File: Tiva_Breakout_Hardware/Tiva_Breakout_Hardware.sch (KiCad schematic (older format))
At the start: 8 parts, among them U1 TM4C129E_Launchpad

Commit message: Finished 30V LEDs and connectors
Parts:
- added D10, D11, D2, D3, D4, D5, D6, D7, D8, D9: 3V3_LED, LED_SMD:LED_0603_1608Metric_Pad1.05x0.95mm_HandSolder, symbol Device:LED_Small
- added R10, R11, R2, R3, R4, R5, R6, R7, R8, R9: 330, Resistor_SMD:R_0603_1608Metric_Pad1.05x0.95mm_HandSolder, symbol Device:R
- 12V_A1: renamed from 12V_B2; value Molex_SL_04 -> PH_2x5; footprint MRDT_Connectors:MOLEX_SL_04_Horizontal -> Connector_PinHeader_1.27mm:PinHeader_2x05_P1.27mm_Vertical; symbol Tiva_Breakout_Hardware-rescue:Molex_SL_04-MRDT_Connectors -> Connector_Generic:Conn_02x05_Odd_Even
- Conn30V_L1: value Molex_SL_07 -> PH_2x5; footprint MRDT_Connectors:MOLEX_SL_07_Horizontal -> Connector_PinHeader_1.27mm:PinHeader_2x05_P1.27mm_Vertical; symbol MRDT_Connectors:Molex_SL_07 -> Connector_Generic:Conn_02x05_Odd_Even
- Conn30V_R1: value Molex_SL_08 -> PH_2x5; footprint MRDT_Connectors:MOLEX_SL_08_Horizontal -> Connector_PinHeader_1.27mm:PinHeader_2x05_P1.27mm_Vertical; symbol MRDT_Connectors:Molex_SL_08 -> Connector_Generic:Conn_02x05_Odd_Even
- ConnPCH_C2: value Molex_SL_10 -> PH_2x5; footprint MRDT_Connectors:MOLEX_SL_10_Horizontal -> Connector_PinHeader_1.27mm:PinHeader_2x05_P1.27mm_Vertical; symbol Tiva_Breakout_Hardware-rescue:Molex_SL_10-MRDT_Connectors -> Connector_Generic:Conn_02x05_Odd_Even
- R1: symbol Device:R_Small -> Device:R
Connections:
- net GND: now also D10.1 (K), D11.1 (K), D2.1 (K), D3.1 (K), D4.1 (K), D5.1 (K), D6.1 (K), D7.1 (K), D8.1 (K), D9.1 (K)
- net AUX_EN: now reaches U1.PC4 (A1_3)
- net AUX_EN: now also Conn30V_R1.6 (Pin_6), R8.2
- net at U1.PC5 (A1_4): no longer 12V_A1.1
- net at U1.PC6 (A1_5): no longer 12V_A1.2
- net at U1.PD3 (A1_7): no longer 12V_A1.4
- net RKT_ISENSE: now reaches U1.PE4 (A1_2)
- net RKT_ISENSE: now also Conn30V_R1.4 (Pin_4)
- net at U1.PE5 (A1_6): no longer 12V_A1.3
- net at U1.PF1 (C1_1): no longer ConnPCH_C2.1
- net at U1.PF2 (C1_2): no longer ConnPCH_C2.2
- net at U1.PF3 (C1_3): no longer ConnPCH_C2.3
- net at U1.PG0 (C1_4): no longer ConnPCH_C2.4
- net at U1.PL0 (C1_7): no longer ConnPCH_C2.7
- net at U1.PL1 (C1_8): no longer ConnPCH_C2.8
- net at U1.PL2 (C1_9): no longer ConnPCH_C2.9
- net at U1.PL3 (C1_10): no longer ConnPCH_C2.10
- net at U1.PL4 (C1_5): no longer ConnPCH_C2.5
- net at U1.PL5 (C1_6): no longer ConnPCH_C2.6
- net M5_EN: now reaches U1.PD5 (A2_6)
- net M5_EN: now also Conn30V_L1.9 (Pin_9), R6.2
- net M1_EN: now reaches U1.PN4 (A2_10)
- net M1_EN: now also Conn30V_L1.8 (Pin_8), R2.2
- net M2_EN: now reaches U1.PN5 (A2_9)
- net M2_EN: now also Conn30V_L1.4 (Pin_4), R3.2
- net M3_EN: now reaches U1.PP4 (A2_8)
- net M3_EN: now also Conn30V_L1.1 (Pin_1), R4.2
- net M4_EN: now reaches U1.PQ0 (A2_7)
- net M4_EN: now also Conn30V_L1.5 (Pin_5), R5.2
- net M3_ISENSE: now reaches Conn30V_L1.2 (Pin_2), U1.PB4 (B2_3)
- net M2_ISENSE: now reaches U1.PB5 (B2_4)
- net M2_ISENSE: now also Conn30V_L1.6 (Pin_6); no longer Conn30V_L1.3
- net M1_ISENSE: now reaches U1.PK0 (B2_5)
- net M1_ISENSE: now also Conn30V_L1.10 (Pin_10); no longer Conn30V_L1.4
- net M5_ISENSE: now reaches U1.PK1 (B2_6)
- net M5_ISENSE: now also Conn30V_L1.7 (Pin_7); no longer Conn30V_L1.5
- net M4_ISENSE: now reaches U1.PK2 (B2_7)
- net M4_ISENSE: now also Conn30V_L1.3 (Pin_3); no longer Conn30V_L1.6
- net at U1.PK3 (B2_8): no longer Conn30V_L1.7
- net 12V_CURR renamed 12V_EN
- net 12V_EN: now also Conn30V_R1.10 (Pin_10), R9.2; no longer Conn30V_R1.4
- net 12V_ON renamed M6_EN
- net M6_EN: now also R11.2
- net AUX_CURR renamed 12V_ISENSE
- net 12V_ISENSE: now also Conn30V_R1.9 (Pin_9); no longer Conn30V_R1.6
- net AUX_ON renamed SP_EN
- net SP_EN: now also Conn30V_R1.7 (Pin_7), R10.2; no longer Conn30V_R1.5
- net EX_CURR renamed AUX_ISENSE
- net AUX_ISENSE: now also Conn30V_R1.8 (Pin_8); no longer Conn30V_R1.2
- net EX_ON renamed M6_ISENSE
- net M6_ISENSE: now also U1.PD7 (B1_7); no longer U1.PM5 (B1_10)
- net RKT_CURR renamed SP_ISENSE
- net SP_ISENSE: now also Conn30V_R1.5 (Pin_5); no longer Conn30V_R1.8
- removed net RKT_ON: Conn30V_R1.7, U1.PD7 (B1_7)
- new net: D2.2 (A), R2.1
- new net: D3.2 (A), R3.1
- new net: D4.2 (A), R4.1
- new net: D5.2 (A), R5.1
- new net: D6.2 (A), R6.1
- new net: D7.2 (A), R7.1
- new net: D8.2 (A), R8.1
- new net: D9.2 (A), R9.1
- new net: D10.2 (A), R10.1
- new net: D11.2 (A), R11.1
- new net RKT_EN: Conn30V_R1.2 (Pin_2), R7.2, U1.PM5 (B1_10)
- no-connect marks 47 -> 39
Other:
- note added: "30V_L"
- note removed: "ACT_CRRT"
- note removed: "ACT_CTRL"
- note removed: "LOG_CRRT"
- note removed: "LOG_CTRL"
- moved on the sheet: U1E, U1F

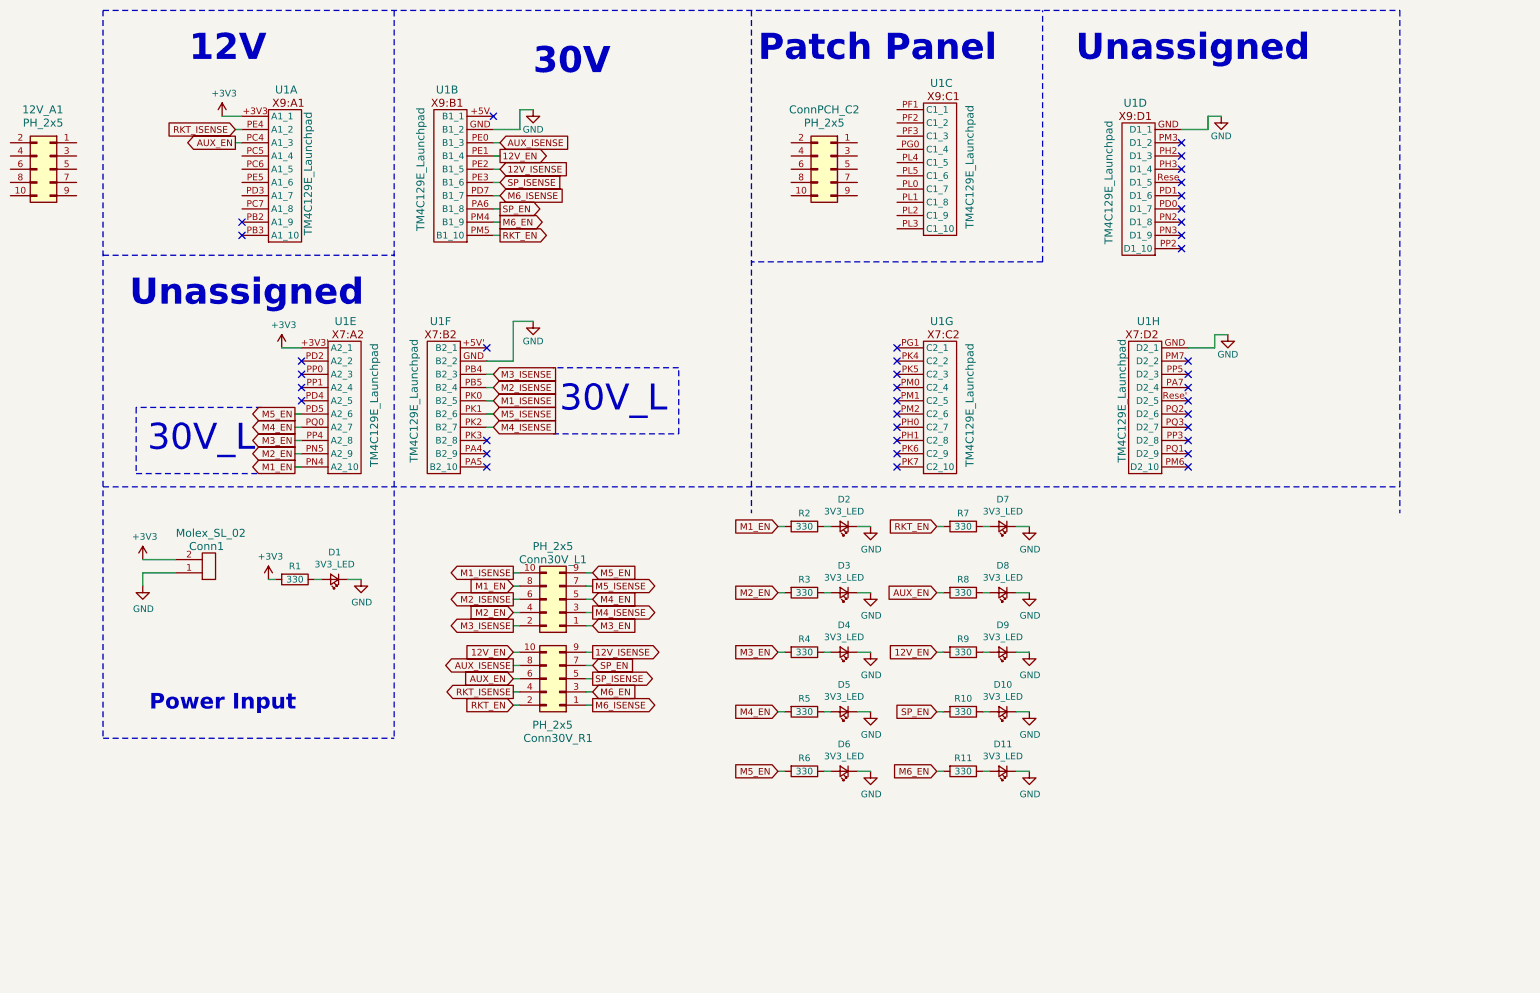
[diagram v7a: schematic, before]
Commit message: Rerouted 30V for readability; routed 12V and LEDs
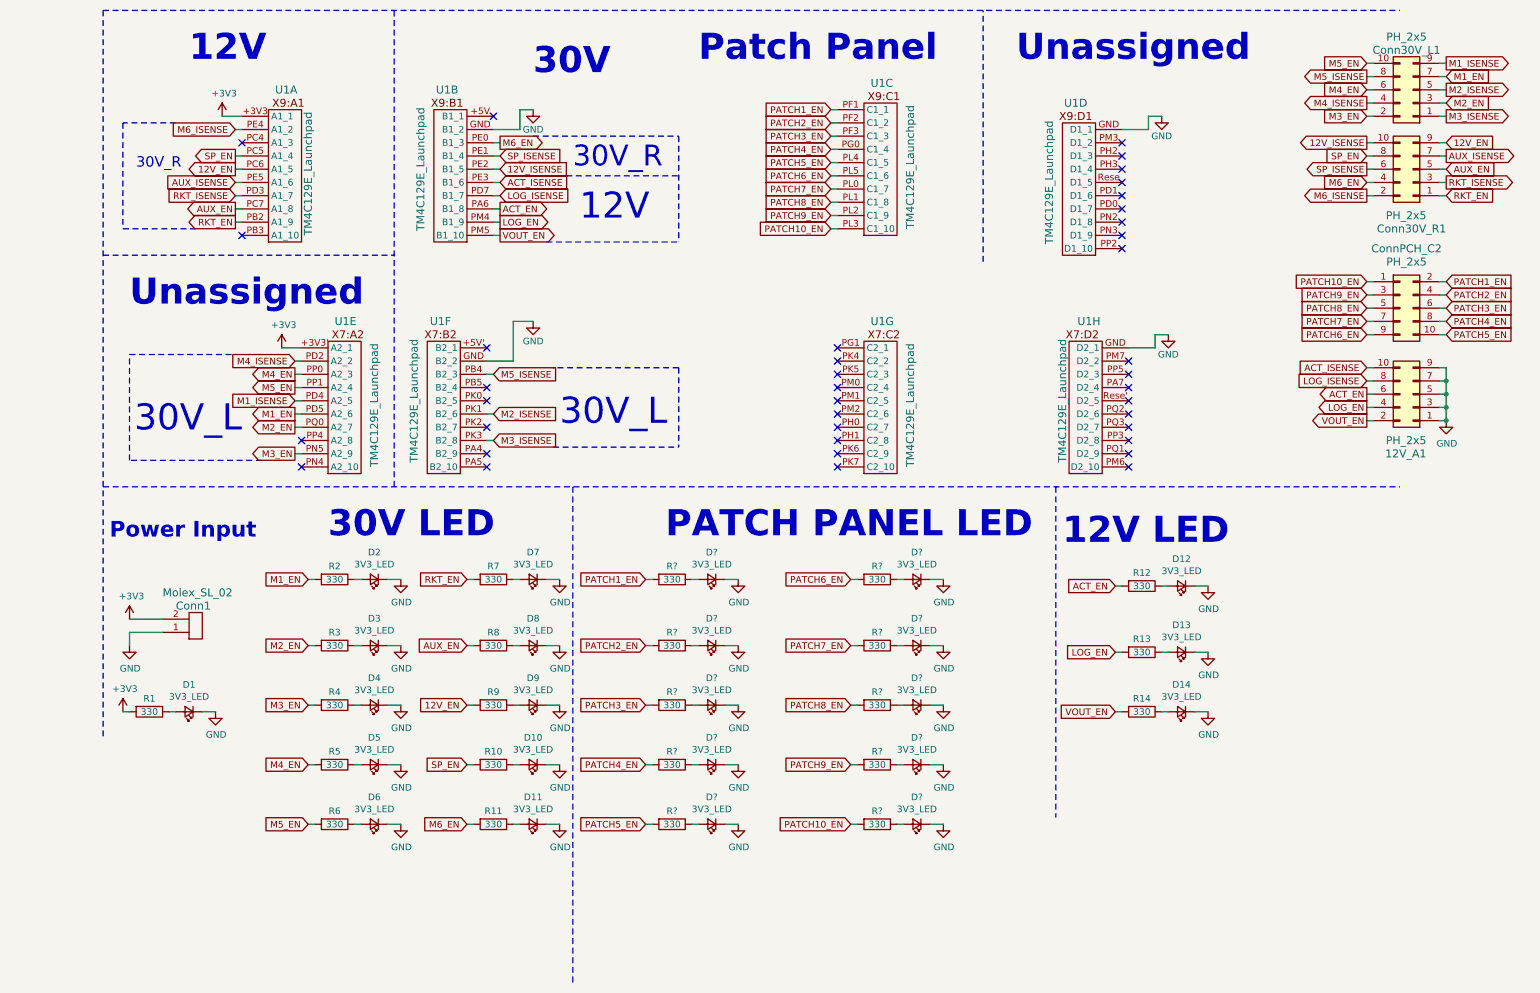
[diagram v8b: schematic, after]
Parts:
- added D12, D13, D14, D? (x10): 3V3_LED, LED_SMD:LED_0603_1608Metric_Pad1.05x0.95mm_HandSolder, symbol Device:LED_Small
- added R12, R13, R14, R? (x10): 330, Resistor_SMD:R_0603_1608Metric_Pad1.05x0.95mm_HandSolder, symbol Device:R
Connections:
- net 12V_EN: now also Conn30V_R1.9 (Pin_9), U1.PC6 (A1_5); no longer Conn30V_R1.10 (Pin_10), U1.PE1 (B1_4)
- net 12V_ISENSE: now also Conn30V_R1.10 (Pin_10); no longer Conn30V_R1.9 (Pin_9)
- net AUX_EN: now also Conn30V_R1.5 (Pin_5), U1.PC7 (A1_8); no longer Conn30V_R1.6 (Pin_6), U1.PC4 (A1_3)
- net AUX_ISENSE: now also Conn30V_R1.7 (Pin_7), U1.PE5 (A1_6); no longer Conn30V_R1.8 (Pin_8), U1.PE0 (B1_3)
- net GND: now also 12V_A1.1 (Pin_1), 12V_A1.3 (Pin_3), 12V_A1.5 (Pin_5), 12V_A1.7 (Pin_7), 12V_A1.9 (Pin_9), D12.1 (K), D13.1 (K), D14.1 (K), D?.1 (K), D?.1 (K), D?.1 (K), D?.1 (K), D?.1 (K), D?.1 (K), D?.1 (K), D?.1 (K), D?.1 (K), D?.1 (K)
- net M1_EN: now also Conn30V_L1.7 (Pin_7), U1.PD5 (A2_6); no longer Conn30V_L1.8 (Pin_8), U1.PN4 (A2_10)
- net M1_ISENSE: now also Conn30V_L1.9 (Pin_9), U1.PD4 (A2_5); no longer Conn30V_L1.10 (Pin_10), U1.PK0 (B2_5)
- net M2_EN: now also Conn30V_L1.3 (Pin_3), U1.PQ0 (A2_7); no longer Conn30V_L1.4 (Pin_4), U1.PN5 (A2_9)
- net M2_ISENSE: now also Conn30V_L1.5 (Pin_5), U1.PK1 (B2_6); no longer Conn30V_L1.6 (Pin_6), U1.PB5 (B2_4)
- net M3_EN: now also Conn30V_L1.2 (Pin_2), U1.PN5 (A2_9); no longer Conn30V_L1.1 (Pin_1), U1.PP4 (A2_8)
- net M3_ISENSE: now also Conn30V_L1.1 (Pin_1), U1.PK3 (B2_8); no longer Conn30V_L1.2 (Pin_2), U1.PB4 (B2_3)
- net M4_EN: now also Conn30V_L1.6 (Pin_6), U1.PP0 (A2_3); no longer Conn30V_L1.5 (Pin_5), U1.PQ0 (A2_7)
- net M4_ISENSE: now also Conn30V_L1.4 (Pin_4), U1.PD2 (A2_2); no longer Conn30V_L1.3 (Pin_3), U1.PK2 (B2_7)
- net M5_EN: now also Conn30V_L1.10 (Pin_10), U1.PP1 (A2_4); no longer Conn30V_L1.9 (Pin_9), U1.PD5 (A2_6)
- net M5_ISENSE: now also Conn30V_L1.8 (Pin_8), U1.PB4 (B2_3); no longer Conn30V_L1.7 (Pin_7), U1.PK1 (B2_6)
- net M6_EN: now also Conn30V_R1.4 (Pin_4), U1.PE0 (B1_3); no longer Conn30V_R1.3 (Pin_3), U1.PM4 (B1_9)
- net M6_ISENSE: now also Conn30V_R1.2 (Pin_2), U1.PE4 (A1_2); no longer Conn30V_R1.1 (Pin_1), U1.PD7 (B1_7)
- net RKT_EN: now also Conn30V_R1.1 (Pin_1), U1.PB2 (A1_9); no longer Conn30V_R1.2 (Pin_2), U1.PM5 (B1_10)
- net RKT_ISENSE: now also Conn30V_R1.3 (Pin_3), U1.PD3 (A1_7); no longer Conn30V_R1.4 (Pin_4), U1.PE4 (A1_2)
- net SP_EN: now also Conn30V_R1.8 (Pin_8), U1.PC5 (A1_4); no longer Conn30V_R1.7 (Pin_7), U1.PA6 (B1_8)
- net SP_ISENSE: now also Conn30V_R1.6 (Pin_6), U1.PE1 (B1_4); no longer Conn30V_R1.5 (Pin_5), U1.PE3 (B1_6)
- net PATCH1_EN: now reaches U1.PF1 (C1_1)
- net PATCH1_EN: now also ConnPCH_C2.2 (Pin_2), R?.2
- net PATCH2_EN: now reaches U1.PF2 (C1_2)
- net PATCH2_EN: now also ConnPCH_C2.4 (Pin_4), R?.2
- net PATCH3_EN: now reaches U1.PF3 (C1_3)
- net PATCH3_EN: now also ConnPCH_C2.6 (Pin_6), R?.2
- net PATCH4_EN: now reaches U1.PG0 (C1_4)
- net PATCH4_EN: now also ConnPCH_C2.8 (Pin_8), R?.2
- net PATCH7_EN: now reaches U1.PL0 (C1_7)
- net PATCH7_EN: now also ConnPCH_C2.7 (Pin_7), R?.2
- net PATCH8_EN: now reaches U1.PL1 (C1_8)
- net PATCH8_EN: now also ConnPCH_C2.5 (Pin_5), R?.2
- net PATCH9_EN: now reaches U1.PL2 (C1_9)
- net PATCH9_EN: now also ConnPCH_C2.3 (Pin_3), R?.2
- net PATCH10_EN: now reaches U1.PL3 (C1_10)
- net PATCH10_EN: now also ConnPCH_C2.1 (Pin_1), R?.2
- net PATCH5_EN: now reaches U1.PL4 (C1_5)
- net PATCH5_EN: now also ConnPCH_C2.10 (Pin_10), R?.2
- net PATCH6_EN: now reaches U1.PL5 (C1_6)
- net PATCH6_EN: now also ConnPCH_C2.9 (Pin_9), R?.2
- net ACT_ISENSE: now reaches 12V_A1.10 (Pin_10)
- net ACT_ISENSE: now also U1.PE3 (B1_6)
- net VOUT_EN: now reaches 12V_A1.2 (Pin_2)
- net VOUT_EN: now also U1.PM5 (B1_10), R14.2
- net LOG_EN: now reaches 12V_A1.4 (Pin_4)
- net LOG_EN: now also U1.PM4 (B1_9), R13.2
- net ACT_EN: now reaches 12V_A1.6 (Pin_6)
- net ACT_EN: now also U1.PA6 (B1_8), R12.2
- net LOG_ISENSE: now reaches 12V_A1.8 (Pin_8)
- net LOG_ISENSE: now also U1.PD7 (B1_7)
- new net: D12.2 (A), R12.1
- new net: D13.2 (A), R13.1
- new net: D14.2 (A), R14.1
- new net: D?.2 (A), R?.1 (x10)
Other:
- note added: "12V LED"
- note added: "30V LED"
- note added: "30V_R"
- note added: "PATCH PANEL LED"
- moved on the sheet: 12V_A1, Conn1, Conn30V_L1, Conn30V_R1, ConnPCH_C2, D1, D10, D11, D2, D3, D4, D5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
